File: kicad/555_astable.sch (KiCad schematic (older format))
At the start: 10 parts, among them U2 555

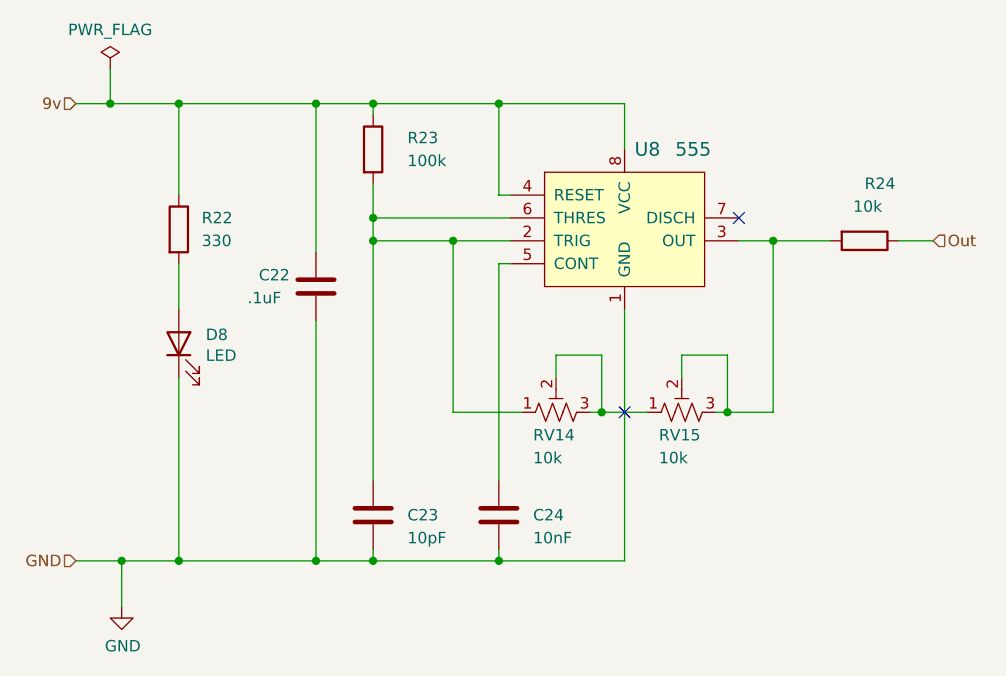
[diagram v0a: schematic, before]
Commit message: Schematic: add switch, more 555s, update TODOs
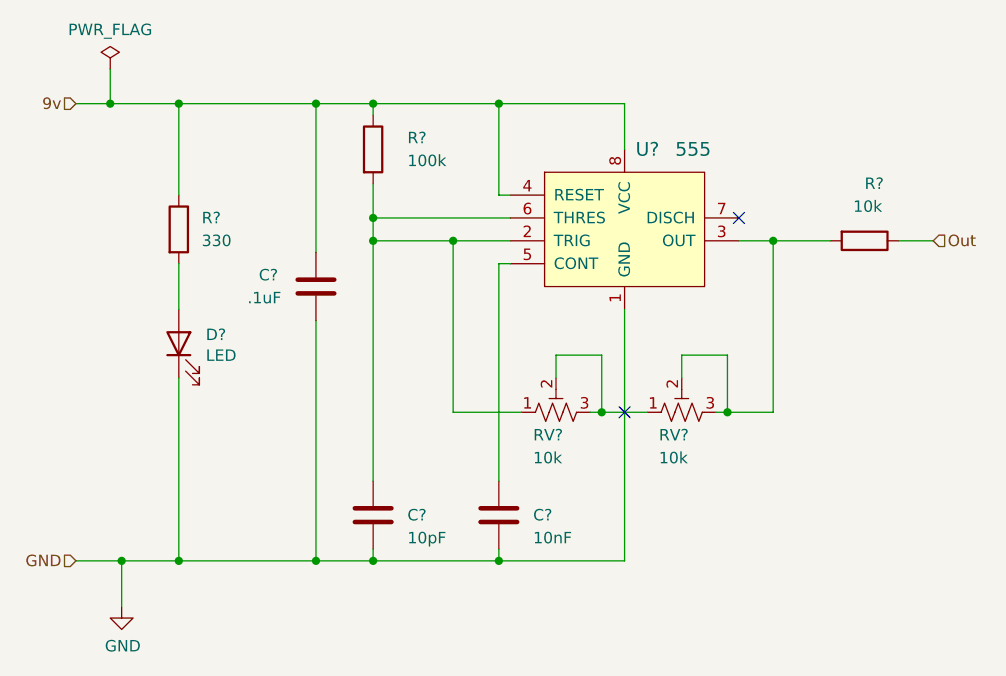
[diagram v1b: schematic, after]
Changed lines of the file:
@@
 $Descr A4 11693 8268
 encoding utf-8
-Sheet 8 14
+Sheet 8 21
 Title ""
 Date ""
@@
 AR Path="/5EF6060B/60F6A68E" Ref="R38"  Part="1"
 AR Path="/5EF7A07F/60F6A68E" Ref="R41"  Part="1"
-F 0 "R23" H 4750 3500 50  0000 L CNN
+AR Path="/5F1B4BC2/60F6A68E" Ref="R?"  Part="1"
+AR Path="/5F1B4BE4/60F6A68E" Ref="R?"  Part="1"
+AR Path="/5F1D8DB1/60F6A68E" Ref="R?"  Part="1"
+AR Path="/5F1D8DD3/60F6A68E" Ref="R?"  Part="1"
+AR Path="/5F1AE585/60F6A68E" Ref="R?"  Part="1"
+AR Path="/5F2156AD/60F6A68E" Ref="R?"  Part="1"
+AR Path="/5F2156CF/60F6A68E" Ref="R?"  Part="1"
+F 0 "R?" H 4750 3500 50  0000 L CNN
 F 1 "100k" H 4750 3400 50  0000 L CNN
 F 2 "Resistor_THT:R_Axial_DIN0204_L3.6mm_D1.6mm_P7.62mm_Horizontal" V 4530 3450 50  0001 C CNN
@@
 AR Path="/5EF6060B/60F6EAC0" Ref="C37"  Part="1"
 AR Path="/5EF7A07F/60F6EAC0" Ref="C40"  Part="1"
-F 0 "C22" H 4100 4100 50  0000 L CNN
+AR Path="/5F1B4BC2/60F6EAC0" Ref="C?"  Part="1"
+AR Path="/5F1B4BE4/60F6EAC0" Ref="C?"  Part="1"
+AR Path="/5F1D8DB1/60F6EAC0" Ref="C?"  Part="1"
+AR Path="/5F1D8DD3/60F6EAC0" Ref="C?"  Part="1"
+AR Path="/5F1AE585/60F6EAC0" Ref="C?"  Part="1"
+AR Path="/5F2156AD/60F6EAC0" Ref="C?"  Part="1"
+AR Path="/5F2156CF/60F6EAC0" Ref="C?"  Part="1"
+F 0 "C?" H 4100 4100 50  0000 L CNN
 F 1 ".1uF" H 4050 4000 50  0000 L CNN
 F 2 "Capacitor_THT:C_Disc_D5.0mm_W2.5mm_P5.00mm" H 4388 3900 50  0001 C CNN
@@
 AR Path="/5EF6060B/60F6A6DA" Ref="U13"  Part="1"
 AR Path="/5EF7A07F/60F6A6DA" Ref="U14"  Part="1"
-F 0 "U8" H 5800 4050 60  0000 C CNN
+AR Path="/5F1B4BC2/60F6A6DA" Ref="U?"  Part="1"
+AR Path="/5F1B4BE4/60F6A6DA" Ref="U?"  Part="1"
+AR Path="/5F1D8DB1/60F6A6DA" Ref="U?"  Part="1"
+AR Path="/5F1D8DD3/60F6A6DA" Ref="U?"  Part="1"
+AR Path="/5F1AE585/60F6A6DA" Ref="U?"  Part="1"
+AR Path="/5F2156AD/60F6A6DA" Ref="U?"  Part="1"
+AR Path="/5F2156CF/60F6A6DA" Ref="U?"  Part="1"
+F 0 "U?" H 5800 4050 60  0000 C CNN
 F 1 "555" H 6000 4050 60  0000 C CNN
 F 2 "Package_DIP:DIP-8_W7.62mm" H 5900 3950 60  0001 L CNN
@@
 AR Path="/5EF6060B/60F6A6C5" Ref="RV25"  Part="1"
 AR Path="/5EF7A07F/60F6A6C5" Ref="RV27"  Part="1"
-F 0 "RV15" V 5850 4700 50  0000 R CNN
+AR Path="/5F1B4BC2/60F6A6C5" Ref="RV?"  Part="1"
+AR Path="/5F1B4BE4/60F6A6C5" Ref="RV?"  Part="1"
+AR Path="/5F1D8DB1/60F6A6C5" Ref="RV?"  Part="1"
+AR Path="/5F1D8DD3/60F6A6C5" Ref="RV?"  Part="1"
+AR Path="/5F1AE585/60F6A6C5" Ref="RV?"  Part="1"
+AR Path="/5F2156AD/60F6A6C5" Ref="RV?"  Part="1"
+AR Path="/5F2156CF/60F6A6C5" Ref="RV?"  Part="1"
+F 0 "RV?" V 5850 4700 50  0000 R CNN
 F 1 "10k" V 5750 4700 50  0000 R CNN
 F 2 "Potentiometer_THT:Potentiometer_Bourns_3386F_Vertical" H 5950 4600 50  0001 C CNN
@@
 AR Path="/5EF6060B/5F59D1F5" Ref="#FLG?"  Part="1"
 AR Path="/5EF7A07F/5F59D1F5" Ref="#FLG?"  Part="1"
+AR Path="/5F1B4BC2/5F59D1F5" Ref="#FLG?"  Part="1"
+AR Path="/5F1B4BE4/5F59D1F5" Ref="#FLG?"  Part="1"
+AR Path="/5F1D8DB1/5F59D1F5" Ref="#FLG?"  Part="1"
+AR Path="/5F1D8DD3/5F59D1F5" Ref="#FLG?"  Part="1"
+AR Path="/5F1AE585/5F59D1F5" Ref="#FLG?"  Part="1"
+AR Path="/5F2156AD/5F59D1F5" Ref="#FLG?"  Part="1"
+AR Path="/5F2156CF/5F59D1F5" Ref="#FLG?"  Part="1"
 F 0 "#FLG?" H 3450 3175 50  0001 C CNN
 F 1 "PWR_FLAG" H 3450 3273 50  0000 C CNN
@@
 AR Path="/5EF6060B/5F5B07DC" Ref="#PWR?"  Part="1"
 AR Path="/5EF7A07F/5F5B07DC" Ref="#PWR?"  Part="1"
+AR Path="/5F1B4BC2/5F5B07DC" Ref="#PWR?"  Part="1"
+AR Path="/5F1B4BE4/5F5B07DC" Ref="#PWR?"  Part="1"
+AR Path="/5F1D8DB1/5F5B07DC" Ref="#PWR?"  Part="1"
+AR Path="/5F1D8DD3/5F5B07DC" Ref="#PWR?"  Part="1"
+AR Path="/5F1AE585/5F5B07DC" Ref="#PWR?"  Part="1"
+AR Path="/5F2156AD/5F5B07DC" Ref="#PWR?"  Part="1"
+AR Path="/5F2156CF/5F5B07DC" Ref="#PWR?"  Part="1"
 F 0 "#PWR?" H 3500 5200 50  0001 C CNN
 F 1 "GND" H 3505 5277 50  0000 C CNN
@@
 AR Path="/5EF6060B/5EFAE830" Ref="R39"  Part="1"
 AR Path="/5EF7A07F/5EFAE830" Ref="R42"  Part="1"
-F 0 "R24" V 6500 3850 50  0000 L CNN
+AR Path="/5F1B4BC2/5EFAE830" Ref="R?"  Part="1"
+AR Path="/5F1B4BE4/5EFAE830" Ref="R?"  Part="1"
+AR Path="/5F1D8DB1/5EFAE830" Ref="R?"  Part="1"
+AR Path="/5F1D8DD3/5EFAE830" Ref="R?"  Part="1"
+AR Path="/5F1AE585/5EFAE830" Ref="R?"  Part="1"
+AR Path="/5F2156AD/5EFAE830" Ref="R?"  Part="1"
+AR Path="/5F2156CF/5EFAE830" Ref="R?"  Part="1"
+F 0 "R?" V 6500 3850 50  0000 L CNN
 F 1 "10k" V 6600 3800 50  0000 L CNN
 F 2 "Resistor_THT:R_Axial_DIN0204_L3.6mm_D1.6mm_P7.62mm_Horizontal" V 6680 3850 50  0001 C CNN
@@
 AR Path="/5EF6060B/5F127BEF" Ref="D13"  Part="1"
 AR Path="/5EF7A07F/5F127BEF" Ref="D14"  Part="1"
-F 0 "D8" V 3789 4182 50  0000 R CNN
+AR Path="/5F1B4BC2/5F127BEF" Ref="D?"  Part="1"
+AR Path="/5F1B4BE4/5F127BEF" Ref="D?"  Part="1"
+AR Path="/5F1D8DB1/5F127BEF" Ref="D?"  Part="1"
+AR Path="/5F1D8DD3/5F127BEF" Ref="D?"  Part="1"
+AR Path="/5F1AE585/5F127BEF" Ref="D?"  Part="1"
+AR Path="/5F2156AD/5F127BEF" Ref="D?"  Part="1"
+AR Path="/5F2156CF/5F127BEF" Ref="D?"  Part="1"
+F 0 "D?" V 3789 4182 50  0000 R CNN
 F 1 "LED" V 3698 4182 50  0000 R CNN
 F 2 "LED_THT:LED_D3.0mm" H 3750 4300 50  0001 C CNN
@@
 AR Path="/5EF6060B/5F127BF5" Ref="R37"  Part="1"
 AR Path="/5EF7A07F/5F127BF5" Ref="R40"  Part="1"
-F 0 "R22" H 3850 3850 50  0000 L CNN
+AR Path="/5F1B4BC2/5F127BF5" Ref="R?"  Part="1"
+AR Path="/5F1B4BE4/5F127BF5" Ref="R?"  Part="1"
+AR Path="/5F1D8DB1/5F127BF5" Ref="R?"  Part="1"
+AR Path="/5F1D8DD3/5F127BF5" Ref="R?"  Part="1"
+AR Path="/5F1AE585/5F127BF5" Ref="R?"  Part="1"
+AR Path="/5F2156AD/5F127BF5" Ref="R?"  Part="1"
+AR Path="/5F2156CF/5F127BF5" Ref="R?"  Part="1"
+F 0 "R?" H 3850 3850 50  0000 L CNN
 F 1 "330" H 3850 3750 50  0000 L CNN
 F 2 "Resistor_THT:R_Axial_DIN0207_L6.3mm_D2.5mm_P2.54mm_Vertical" V 3680 3800 50  0001 C CNN
@@
 AR Path="/5EF6060B/5F13ACF1" Ref="RV24"  Part="1"
 AR Path="/5EF7A07F/5F13ACF1" Ref="RV26"  Part="1"
-F 0 "RV14" V 5300 4700 50  0000 R CNN
+AR Path="/5F1B4BC2/5F13ACF1" Ref="RV?"  Part="1"
+AR Path="/5F1B4BE4/5F13ACF1" Ref="RV?"  Part="1"
+AR Path="/5F1D8DB1/5F13ACF1" Ref="RV?"  Part="1"
+AR Path="/5F1D8DD3/5F13ACF1" Ref="RV?"  Part="1"
+AR Path="/5F1AE585/5F13ACF1" Ref="RV?"  Part="1"
+AR Path="/5F2156AD/5F13ACF1" Ref="RV?"  Part="1"
+AR Path="/5F2156CF/5F13ACF1" Ref="RV?"  Part="1"
+F 0 "RV?" V 5300 4700 50  0000 R CNN
 F 1 "10k" V 5200 4700 50  0000 R CNN
 F 2 "Potentiometer_THT:Potentiometer_Bourns_3296W_Vertical" H 5400 4600 50  0001 C CNN
@@
 AR Path="/5EF6060B/60F6A6A0" Ref="C39"  Part="1"
 AR Path="/5EF7A07F/60F6A6A0" Ref="C42"  Part="1"
-F 0 "C24" H 5300 5050 50  0000 L CNN
+AR Path="/5F1B4BC2/60F6A6A0" Ref="C?"  Part="1"
+AR Path="/5F1B4BE4/60F6A6A0" Ref="C?"  Part="1"
+AR Path="/5F1D8DB1/60F6A6A0" Ref="C?"  Part="1"
+AR Path="/5F1D8DD3/60F6A6A0" Ref="C?"  Part="1"
+AR Path="/5F1AE585/60F6A6A0" Ref="C?"  Part="1"
+AR Path="/5F2156AD/60F6A6A0" Ref="C?"  Part="1"
+AR Path="/5F2156CF/60F6A6A0" Ref="C?"  Part="1"
+F 0 "C?" H 5300 5050 50  0000 L CNN
 F 1 "10nF" H 5300 4950 50  0000 L CNN
 F 2 "Capacitor_THT:C_Disc_D5.0mm_W2.5mm_P5.00mm" H 5188 4900 50  0001 C CNN
@@
 AR Path="/5EF6060B/60F6A69A" Ref="C38"  Part="1"
 AR Path="/5EF7A07F/60F6A69A" Ref="C41"  Part="1"
-F 0 "C23" H 4750 5050 50  0000 L CNN
+AR Path="/5F1B4BC2/60F6A69A" Ref="C?"  Part="1"
+AR Path="/5F1B4BE4/60F6A69A" Ref="C?"  Part="1"
+AR Path="/5F1D8DB1/60F6A69A" Ref="C?"  Part="1"
+AR Path="/5F1D8DD3/60F6A69A" Ref="C?"  Part="1"
+AR Path="/5F1AE585/60F6A69A" Ref="C?"  Part="1"
+AR Path="/5F2156AD/60F6A69A" Ref="C?"  Part="1"
+AR Path="/5F2156CF/60F6A69A" Ref="C?"  Part="1"
+F 0 "C?" H 4750 5050 50  0000 L CNN
 F 1 "10pF" H 4750 4950 50  0000 L CNN
 F 2 "Capacitor_THT:C_Disc_D5.0mm_W2.5mm_P5.00mm" H 4638 4900 50  0001 C CNN

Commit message: Reverse fine tuning rotation
These pots are countinerintuitive
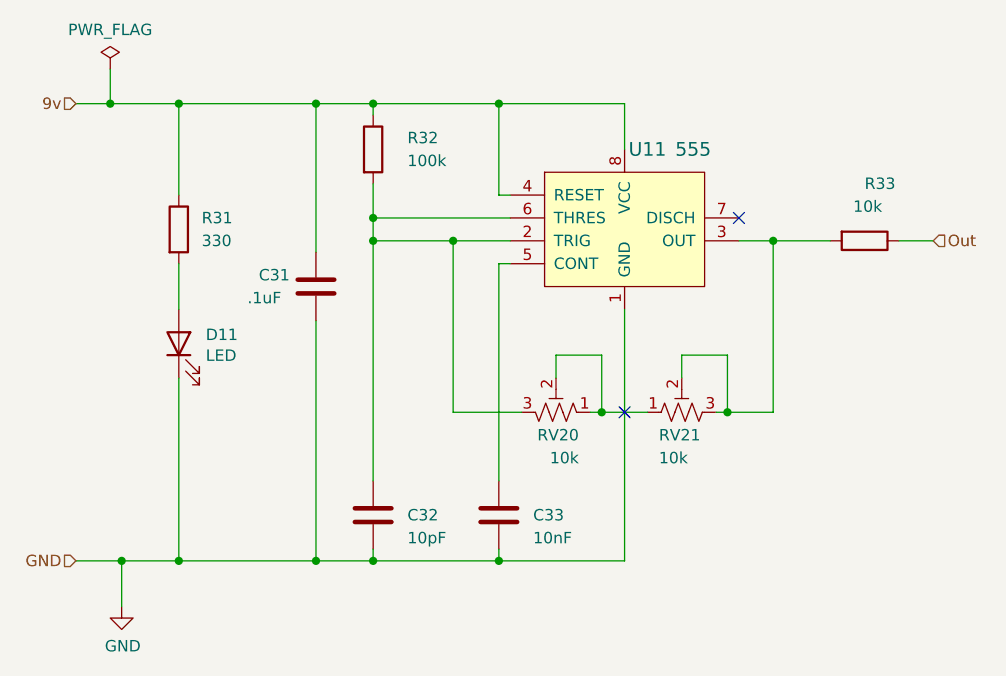
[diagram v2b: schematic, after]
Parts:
- RV2: Description (none) -> Fine
- RV3: Description (none) -> Course
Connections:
- net at C5.1, R5.2, U2.2 (TRIG)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: now also RV2.3; no longer RV2.1
- net at RV2.2, RV3.1: now also RV2.1; no longer RV2.3

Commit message: Fix swapped 386 POW/GND pins
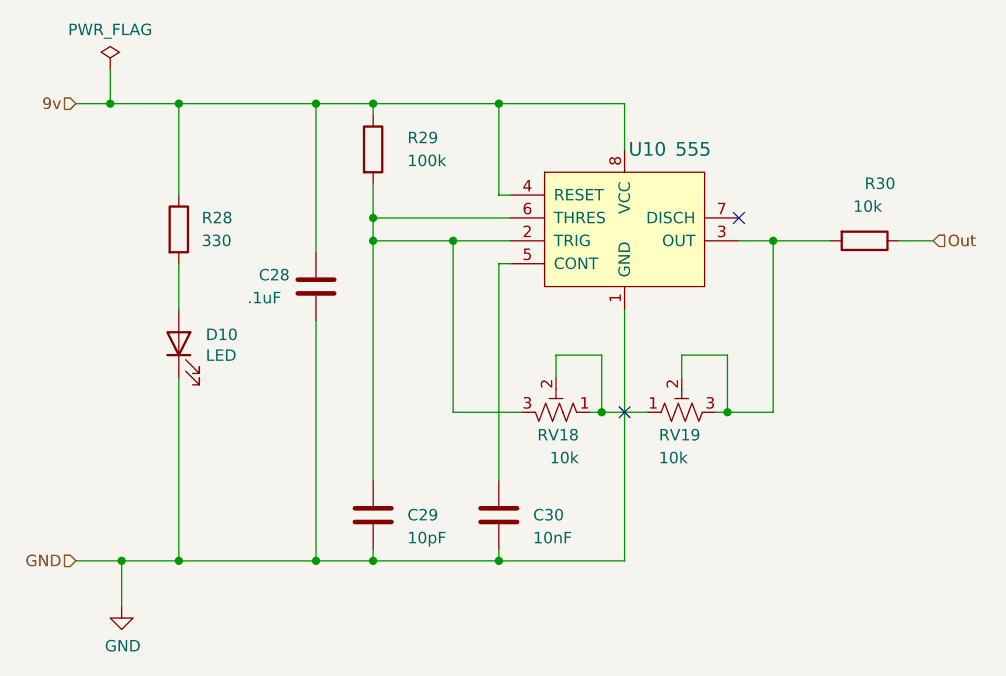
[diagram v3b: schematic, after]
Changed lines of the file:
@@
 $Descr A4 11693 8268
 encoding utf-8
-Sheet 11 21
+Sheet 10 21
 Title ""
 Date ""
@@
 AR Path="/5F2156AD/60F6A68E" Ref="R?"  Part="1"
 AR Path="/5F2156CF/60F6A68E" Ref="R?"  Part="1"
-F 0 "R32" H 4750 3500 50  0000 L CNN
+F 0 "R29" H 4750 3500 50  0000 L CNN
 F 1 "100k" H 4750 3400 50  0000 L CNN
 F 2 "Resistor_THT:R_Axial_DIN0204_L3.6mm_D1.6mm_P7.62mm_Horizontal" V 4530 3450 50  0001 C CNN
@@
 AR Path="/5F2156AD/60F6EAC0" Ref="C?"  Part="1"
 AR Path="/5F2156CF/60F6EAC0" Ref="C?"  Part="1"
-F 0 "C31" H 4100 4100 50  0000 L CNN
+F 0 "C28" H 4100 4100 50  0000 L CNN
 F 1 ".1uF" H 4050 4000 50  0000 L CNN
 F 2 "Capacitor_THT:C_Disc_D5.0mm_W2.5mm_P5.00mm" H 4388 3900 50  0001 C CNN
@@
 AR Path="/5F2156AD/60F6A6DA" Ref="U?"  Part="1"
 AR Path="/5F2156CF/60F6A6DA" Ref="U?"  Part="1"
-F 0 "U11" H 5800 4050 60  0000 C CNN
+F 0 "U10" H 5800 4050 60  0000 C CNN
 F 1 "555" H 6000 4050 60  0000 C CNN
 F 2 "Package_DIP:DIP-8_W7.62mm" H 5900 3950 60  0001 L CNN
@@
 AR Path="/5F2156AD/60F6A6C5" Ref="RV?"  Part="1"
 AR Path="/5F2156CF/60F6A6C5" Ref="RV?"  Part="1"
-F 0 "RV21" V 5850 4700 50  0000 R CNN
+F 0 "RV19" V 5850 4700 50  0000 R CNN
 F 1 "10k" V 5750 4700 50  0000 R CNN
 F 2 "Potentiometer_THT:Potentiometer_Bourns_3386F_Vertical" H 5950 4600 50  0001 C CNN
@@
 AR Path="/5F2156AD/5EFAE830" Ref="R?"  Part="1"
 AR Path="/5F2156CF/5EFAE830" Ref="R?"  Part="1"
-F 0 "R33" V 6500 3850 50  0000 L CNN
+F 0 "R30" V 6500 3850 50  0000 L CNN
 F 1 "10k" V 6600 3800 50  0000 L CNN
 F 2 "Resistor_THT:R_Axial_DIN0204_L3.6mm_D1.6mm_P7.62mm_Horizontal" V 6680 3850 50  0001 C CNN
@@
 AR Path="/5F2156AD/5F127BEF" Ref="D?"  Part="1"
 AR Path="/5F2156CF/5F127BEF" Ref="D?"  Part="1"
-F 0 "D11" V 3789 4182 50  0000 R CNN
+F 0 "D10" V 3789 4182 50  0000 R CNN
 F 1 "LED" V 3698 4182 50  0000 R CNN
 F 2 "LED_THT:LED_D3.0mm" H 3750 4300 50  0001 C CNN
@@
 AR Path="/5F2156AD/5F127BF5" Ref="R?"  Part="1"
 AR Path="/5F2156CF/5F127BF5" Ref="R?"  Part="1"
-F 0 "R31" H 3850 3850 50  0000 L CNN
+F 0 "R28" H 3850 3850 50  0000 L CNN
 F 1 "330" H 3850 3750 50  0000 L CNN
 F 2 "Resistor_THT:R_Axial_DIN0207_L6.3mm_D2.5mm_P2.54mm_Vertical" V 3680 3800 50  0001 C CNN
@@
 AR Path="/5F2156AD/60F6A6A0" Ref="C?"  Part="1"
 AR Path="/5F2156CF/60F6A6A0" Ref="C?"  Part="1"
-F 0 "C33" H 5300 5050 50  0000 L CNN
+F 0 "C30" H 5300 5050 50  0000 L CNN
 F 1 "10nF" H 5300 4950 50  0000 L CNN
 F 2 "Capacitor_THT:C_Disc_D5.0mm_W2.5mm_P5.00mm" H 5188 4900 50  0001 C CNN
@@
 AR Path="/5F2156AD/60F6A69A" Ref="C?"  Part="1"
 AR Path="/5F2156CF/60F6A69A" Ref="C?"  Part="1"
-F 0 "C32" H 4750 5050 50  0000 L CNN
+F 0 "C29" H 4750 5050 50  0000 L CNN
 F 1 "10pF" H 4750 4950 50  0000 L CNN
 F 2 "Capacitor_THT:C_Disc_D5.0mm_W2.5mm_P5.00mm" H 4638 4900 50  0001 C CNN
@@
 AR Path="/5F2156AD/5F13ACF1" Ref="RV?"  Part="1"
 AR Path="/5F2156CF/5F13ACF1" Ref="RV?"  Part="1"
-F 0 "RV20" V 5300 4700 50  0000 R CNN
+F 0 "RV18" V 5300 4700 50  0000 R CNN
 F 1 "10k" V 5200 4700 50  0000 R CNN
 F 2 "Potentiometer_THT:Potentiometer_Bourns_3296W_Vertical" H 5400 4600 50  0001 C CNN

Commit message: Update values: timing cap, tuning pots, log resistor
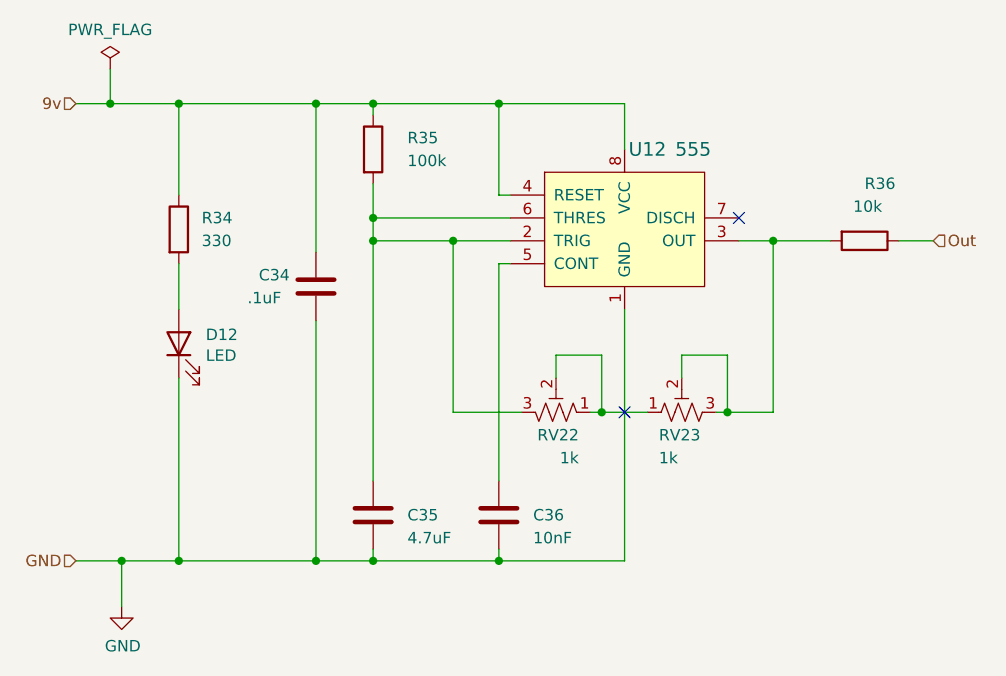
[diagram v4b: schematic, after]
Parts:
- C5: value 10pF -> 4.7uF; Description (none) -> Timing
- RV2, RV3: value 10k -> 1k
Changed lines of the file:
@@
 $Descr A4 11693 8268
 encoding utf-8
-Sheet 10 21
+Sheet 12 21
 Title ""
 Date ""
@@
 AR Path="/5F2156AD/60F6A68E" Ref="R?"  Part="1"
 AR Path="/5F2156CF/60F6A68E" Ref="R?"  Part="1"
-F 0 "R29" H 4750 3500 50  0000 L CNN
+F 0 "R35" H 4750 3500 50  0000 L CNN
 F 1 "100k" H 4750 3400 50  0000 L CNN
 F 2 "Resistor_THT:R_Axial_DIN0204_L3.6mm_D1.6mm_P7.62mm_Horizontal" V 4530 3450 50  0001 C CNN
@@
 AR Path="/5F2156AD/60F6EAC0" Ref="C?"  Part="1"
 AR Path="/5F2156CF/60F6EAC0" Ref="C?"  Part="1"
-F 0 "C28" H 4100 4100 50  0000 L CNN
+F 0 "C34" H 4100 4100 50  0000 L CNN
 F 1 ".1uF" H 4050 4000 50  0000 L CNN
 F 2 "Capacitor_THT:C_Disc_D5.0mm_W2.5mm_P5.00mm" H 4388 3900 50  0001 C CNN
@@
 AR Path="/5F2156AD/60F6A6DA" Ref="U?"  Part="1"
 AR Path="/5F2156CF/60F6A6DA" Ref="U?"  Part="1"
-F 0 "U10" H 5800 4050 60  0000 C CNN
+F 0 "U12" H 5800 4050 60  0000 C CNN
 F 1 "555" H 6000 4050 60  0000 C CNN
 F 2 "Package_DIP:DIP-8_W7.62mm" H 5900 3950 60  0001 L CNN
@@
 AR Path="/5F2156AD/60F6A6C5" Ref="RV?"  Part="1"
 AR Path="/5F2156CF/60F6A6C5" Ref="RV?"  Part="1"
-F 0 "RV19" V 5850 4700 50  0000 R CNN
-F 1 "10k" V 5750 4700 50  0000 R CNN
+F 0 "RV23" V 5850 4700 50  0000 R CNN
+F 1 "1k" V 5750 4700 50  0000 R CNN
 F 2 "Potentiometer_THT:Potentiometer_Bourns_3386F_Vertical" H 5950 4600 50  0001 C CNN
 F 3 "~" H 5950 4600 50  0001 C CNN
@@
 AR Path="/5F2156AD/5EFAE830" Ref="R?"  Part="1"
 AR Path="/5F2156CF/5EFAE830" Ref="R?"  Part="1"
-F 0 "R30" V 6500 3850 50  0000 L CNN
+F 0 "R36" V 6500 3850 50  0000 L CNN
 F 1 "10k" V 6600 3800 50  0000 L CNN
 F 2 "Resistor_THT:R_Axial_DIN0204_L3.6mm_D1.6mm_P7.62mm_Horizontal" V 6680 3850 50  0001 C CNN
@@
 AR Path="/5F2156AD/5F127BEF" Ref="D?"  Part="1"
 AR Path="/5F2156CF/5F127BEF" Ref="D?"  Part="1"
-F 0 "D10" V 3789 4182 50  0000 R CNN
+F 0 "D12" V 3789 4182 50  0000 R CNN
 F 1 "LED" V 3698 4182 50  0000 R CNN
 F 2 "LED_THT:LED_D3.0mm" H 3750 4300 50  0001 C CNN
@@
 AR Path="/5F2156AD/5F127BF5" Ref="R?"  Part="1"
 AR Path="/5F2156CF/5F127BF5" Ref="R?"  Part="1"
-F 0 "R28" H 3850 3850 50  0000 L CNN
+F 0 "R34" H 3850 3850 50  0000 L CNN
 F 1 "330" H 3850 3750 50  0000 L CNN
 F 2 "Resistor_THT:R_Axial_DIN0207_L6.3mm_D2.5mm_P2.54mm_Vertical" V 3680 3800 50  0001 C CNN
@@
 AR Path="/5F2156AD/60F6A6A0" Ref="C?"  Part="1"
 AR Path="/5F2156CF/60F6A6A0" Ref="C?"  Part="1"
-F 0 "C30" H 5300 5050 50  0000 L CNN
+F 0 "C36" H 5300 5050 50  0000 L CNN
 F 1 "10nF" H 5300 4950 50  0000 L CNN
 F 2 "Capacitor_THT:C_Disc_D5.0mm_W2.5mm_P5.00mm" H 5188 4900 50  0001 C CNN
@@
 AR Path="/5F2156AD/60F6A69A" Ref="C?"  Part="1"
 AR Path="/5F2156CF/60F6A69A" Ref="C?"  Part="1"
-F 0 "C29" H 4750 5050 50  0000 L CNN
-F 1 "10pF" H 4750 4950 50  0000 L CNN
+F 0 "C35" H 4750 5050 50  0000 L CNN
+F 1 "4.7uF" H 4750 4950 50  0000 L CNN
 F 2 "Capacitor_THT:C_Disc_D5.0mm_W2.5mm_P5.00mm" H 4638 4900 50  0001 C CNN
 F 3 "~" H 4600 5050 50  0001 C CNN
+F 4 "Timing" H 4600 5050 50  0001 C CNN "Description"
 	1    4600 5050
 	1    0    0    -1
@@
 AR Path="/5F2156AD/5F13ACF1" Ref="RV?"  Part="1"
 AR Path="/5F2156CF/5F13ACF1" Ref="RV?"  Part="1"
-F 0 "RV18" V 5300 4700 50  0000 R CNN
-F 1 "10k" V 5200 4700 50  0000 R CNN
+F 0 "RV22" V 5300 4700 50  0000 R CNN
+F 1 "1k" V 5200 4700 50  0000 R CNN
 F 2 "Potentiometer_THT:Potentiometer_Bourns_3296W_Vertical" H 5400 4600 50  0001 C CNN
 F 3 "~" H 5400 4600 50  0001 C CNN
